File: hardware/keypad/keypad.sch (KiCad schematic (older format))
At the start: 21 parts, among them J1 HEADER_6, J2 HEADER_6, J3 ISP, J4 I2C, SW1 SW_PUSH, X1 CRYSTAL

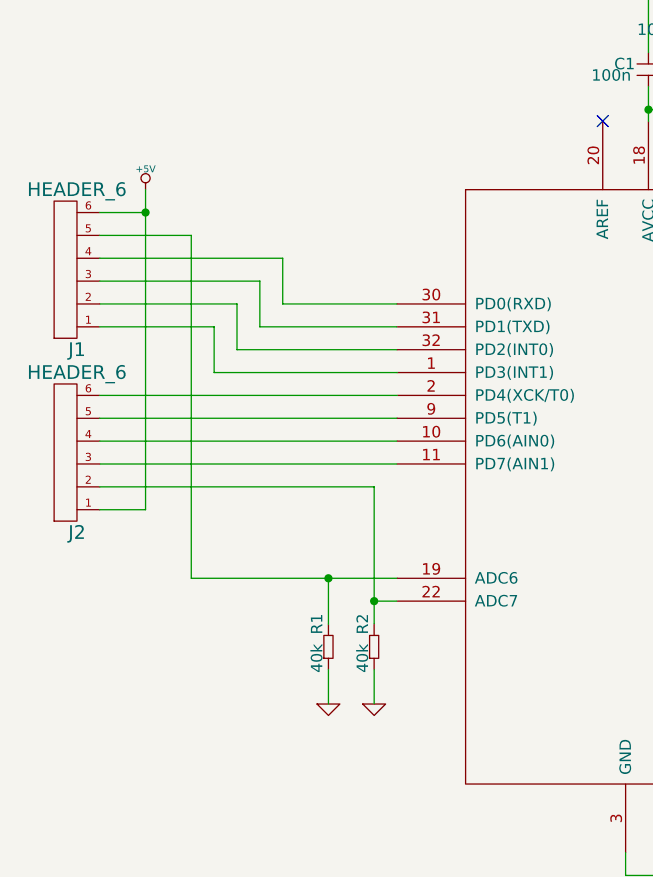
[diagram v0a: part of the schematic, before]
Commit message: First revision of keypad PCB.
http://i.imgur.com/pNjvT0o.jpg
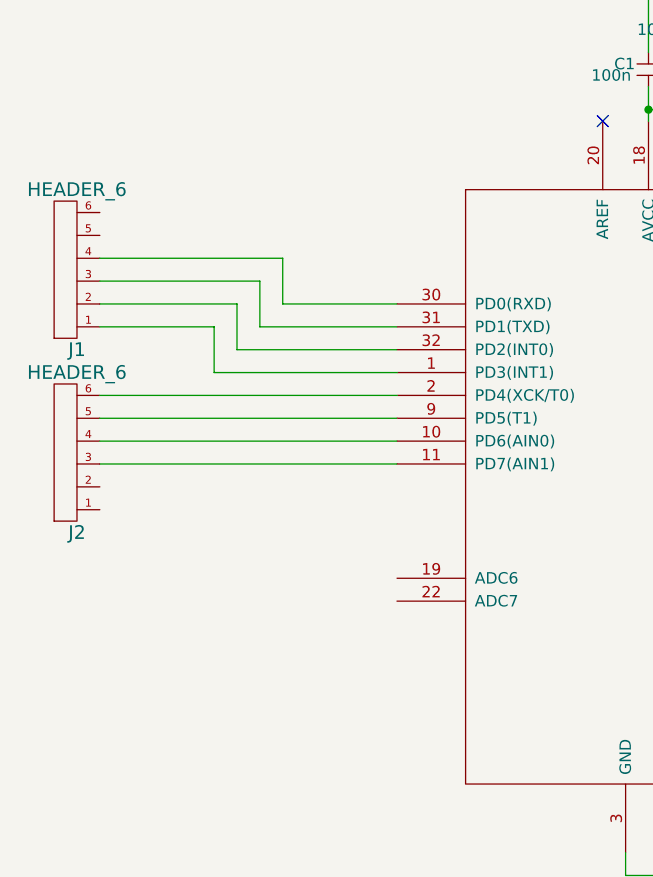
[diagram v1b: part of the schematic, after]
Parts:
- removed R1, R2: 40k, symbol R
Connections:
- wire segments 101 -> 89
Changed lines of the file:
@@
 	3300 2950 2800 2950
-$Comp
-L R R2
-U 1 1 52346CDB
-P 4000 4350
-F 0 "R2" V 4050 4250 50  0000 C CNN
-F 1 "40k" V 4050 4400 50  0000 C CNN
-F 2 "" H 4000 4350 60  0000 C CNN
-F 3 "" H 4000 4350 60  0000 C CNN
-	1    4000 4350
-	-1   0    0    1
-$EndComp
-$Comp
-L R R1
-U 1 1 52346CE6
-P 3800 4350
-F 0 "R1" V 3850 4250 50  0000 C CNN
-F 1 "40k" V 3850 4400 50  0000 C CNN
-F 2 "" H 3800 4350 60  0000 C CNN
-F 3 "" H 3800 4350 60  0000 C CNN
-	1    3800 4350
-	-1   0    0    1
-$EndComp
-Wire Wire Line
-	3200 4050 4100 4050
-Wire Wire Line
-	3800 4050 3800 4250
-Wire Wire Line
-	4100 4150 4000 4150
-Wire Wire Line
-	4000 3650 4000 4250
-$Comp
-L GND #PWR09
-U 1 1 52346DCA
-P 4000 4600
-F 0 "#PWR09" H 4000 4600 30  0001 C CNN
-F 1 "GND" H 4000 4530 30  0001 C CNN
-F 2 "" H 4000 4600 60  0000 C CNN
-F 3 "" H 4000 4600 60  0000 C CNN
-	1    4000 4600
-	1    0    0    -1
-$EndComp
-$Comp
-L GND #PWR010
-U 1 1 52346DD5
-P 3800 4600
-F 0 "#PWR010" H 3800 4600 30  0001 C CNN
-F 1 "GND" H 3800 4530 30  0001 C CNN
-F 2 "" H 3800 4600 60  0000 C CNN
-F 3 "" H 3800 4600 60  0000 C CNN
-	1    3800 4600
-	1    0    0    -1
-$EndComp
-Wire Wire Line
-	3800 4450 3800 4600
-Wire Wire Line
-	4000 4450 4000 4600
-Wire Wire Line
-	2800 2550 3200 2550
-Wire Wire Line
-	3200 2550 3200 4050
-Connection ~ 3800 4050
-Wire Wire Line
-	2800 3650 4000 3650
-Connection ~ 4000 4150
-$Comp
-L +5V #PWR011
-U 1 1 52346F1B
-P 3000 2350
-F 0 "#PWR011" H 3000 2440 20  0001 C CNN
-F 1 "+5V" H 3000 2440 30  0000 C CNN
-F 2 "" H 3000 2350 60  0000 C CNN
-F 3 "" H 3000 2350 60  0000 C CNN
-	1    3000 2350
-	1    0    0    -1
-$EndComp
-Wire Wire Line
-	2800 3750 3000 3750
-Wire Wire Line
-	3000 3750 3000 2350
-Wire Wire Line
-	2800 2450 3000 2450
-Connection ~ 3000 2450
 $Comp
 L HEADER_3X2 J3
